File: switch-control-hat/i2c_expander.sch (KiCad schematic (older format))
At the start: 2 parts, among them U1 MCP23017_SO

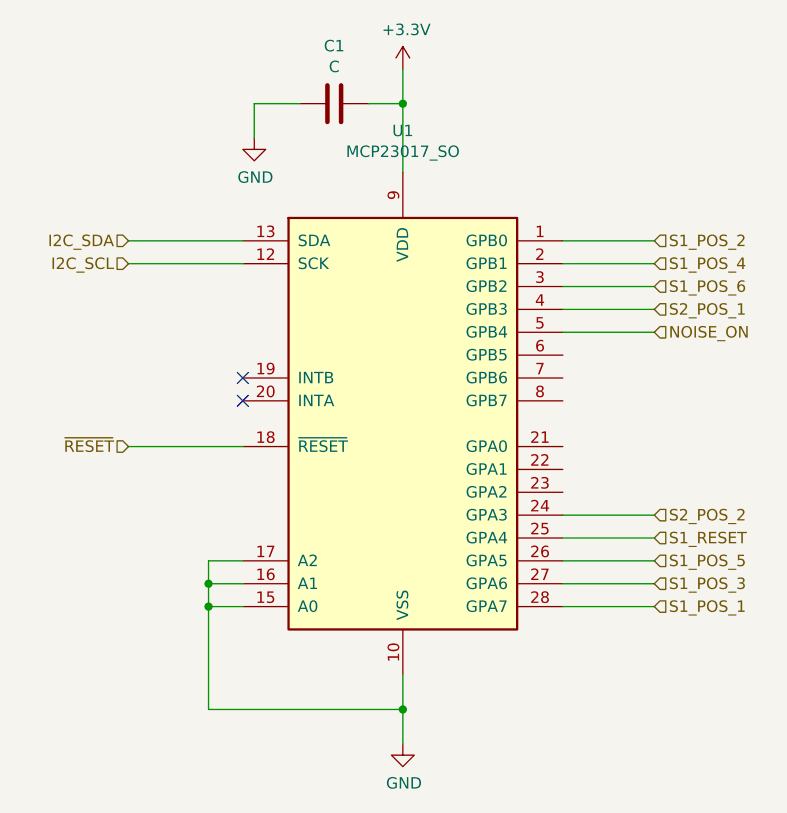
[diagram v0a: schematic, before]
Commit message: Fixed ERC and DRC errors
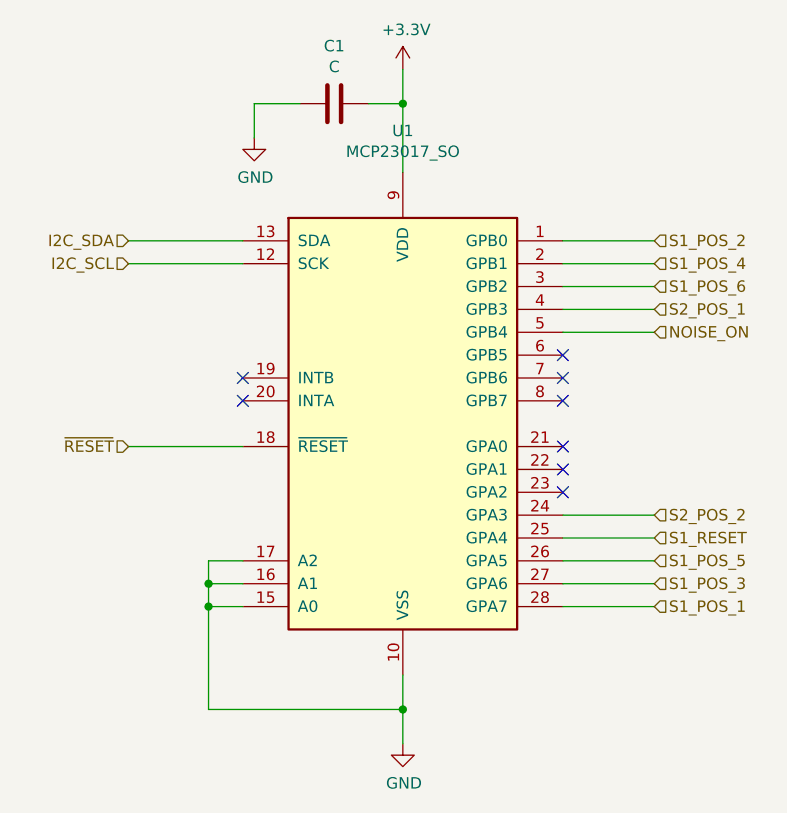
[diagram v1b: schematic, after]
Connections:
- no-connect marks 2 -> 8
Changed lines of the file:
@@
 Sheet 6 6
 Title ""
-Date ""
+Date "2020-03-06"
 Rev ""
 Comp ""
@@
 Text HLabel 6950 3500 2    50   Input ~ 0
 S2_POS_1
+NoConn ~ 6550 3700
+NoConn ~ 6550 3800
+NoConn ~ 6550 3900
+NoConn ~ 6550 4100
+NoConn ~ 6550 4200
+NoConn ~ 6550 4300
 $EndSCHEMATC
